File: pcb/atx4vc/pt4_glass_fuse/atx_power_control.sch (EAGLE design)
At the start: 62 parts, among them IC2 REG1117, IC3 STM32F042F4, IC4 MY_7905DT, J1 ATX24RH, SW1 324_SW, SW2 324_SW, SW3 324_SW, SW4 324_SW, SW5 324_SW, SW7 324_SW, U1 USBC_16P, U2 USBC_16P

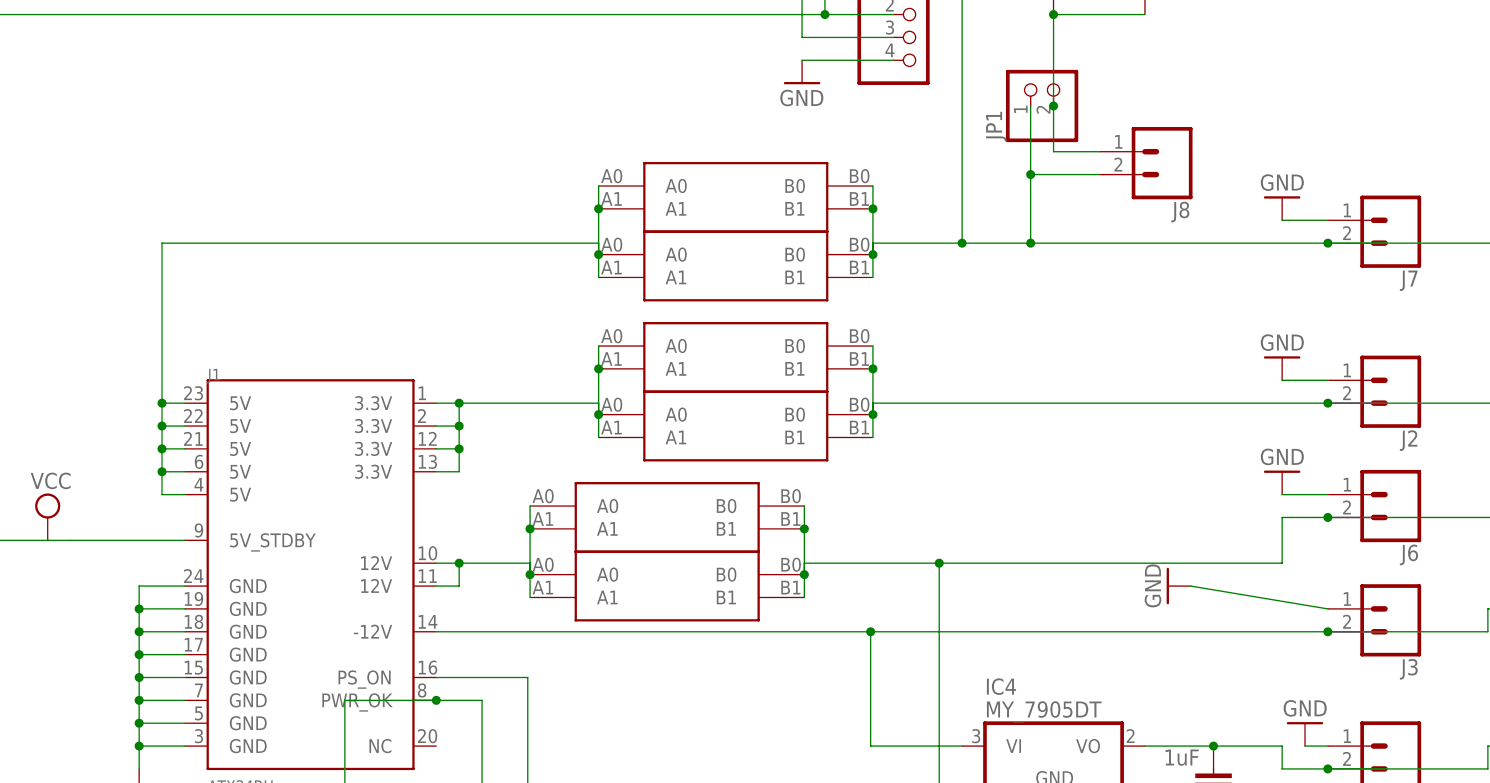
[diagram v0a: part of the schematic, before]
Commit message: updated PCB to use car fuse holder
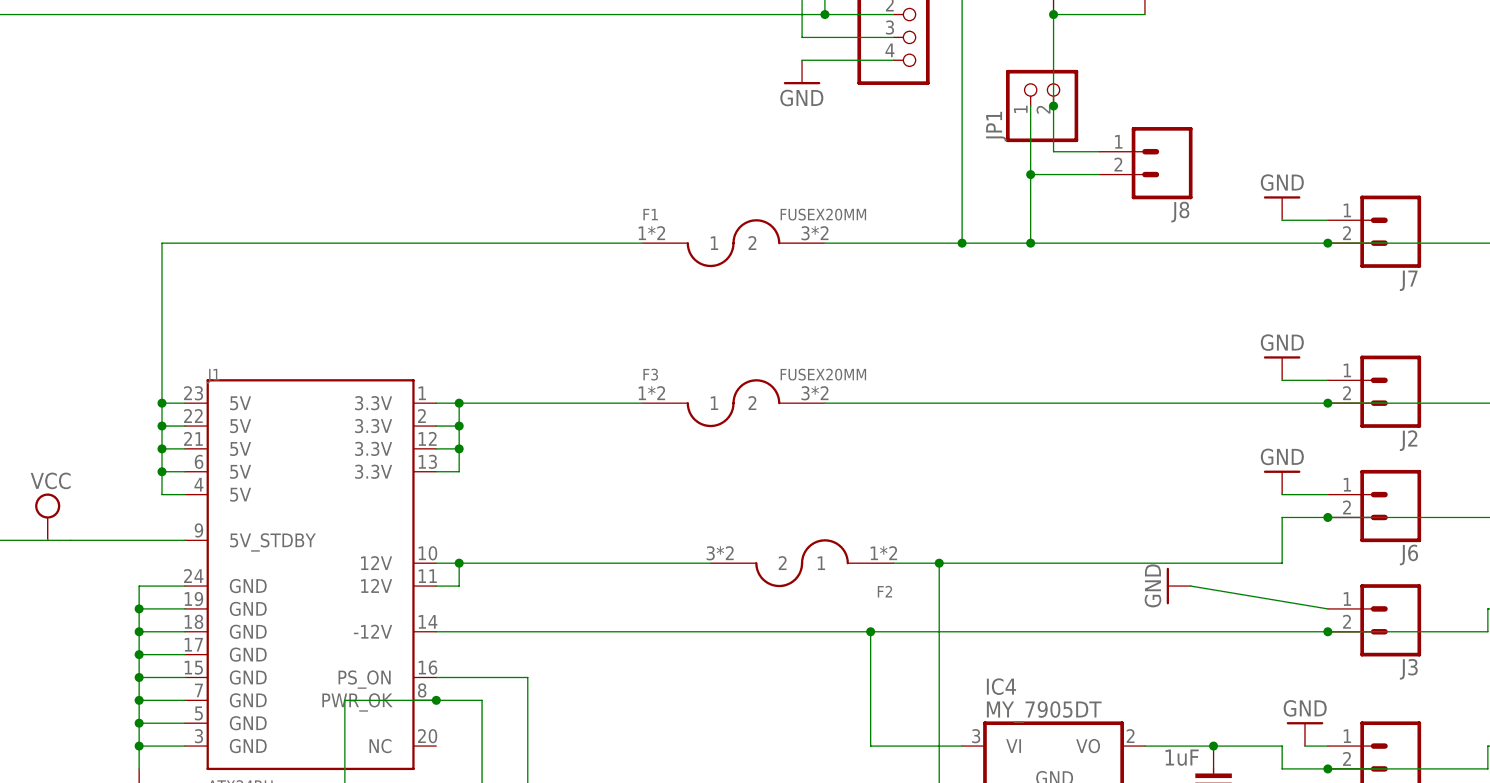
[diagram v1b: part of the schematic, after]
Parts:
- removed U$4, U$6, U$9: FUSE_HOLDER, atx_power_control:FUSE_HOLDER
- removed U$5, U$7, U$8: CAR_FUSE_HOLDER3IN1, atx_power_control:CAR_FUSE_HOLDER3IN1
- added F1, F2, F3: FUSEX20MM, atx_power_control:FUSEX20MM
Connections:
- removed net N$15: J6.2, JP2.3, LED5.A, U$4.B0, U$4.B1, U$5.B0, U$5.B1
- new net N$19: F3.2, J2.2, LED6.A
- net N$10: now also F1.1; no longer U$8.A0, U$8.A1, U$9.A0, U$9.A1
- net N$14: now also F3.1; no longer U$6.A0, U$6.A1, U$7.A0, U$7.A1
- net N$16: now also F2.1, J6.2, JP2.3, LED5.A; no longer J2.2, LED6.A, U$6.B0, U$6.B1, U$7.B0, U$7.B1
- net N$21: now also F2.2; no longer U$4.A0, U$4.A1, U$5.A0, U$5.A1
- net N$30: now also F1.2; no longer U$8.B0, U$8.B1, U$9.B0, U$9.B1
